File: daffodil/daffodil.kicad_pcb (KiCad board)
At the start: 2 copper layers, 70.7 x 53.3 mm, 8 parts, among them J1 NEIGHBOR1, J2 NEIGHBOR2, J7 BONUS_ROW, P1 GREATFET-PROTO-AREA

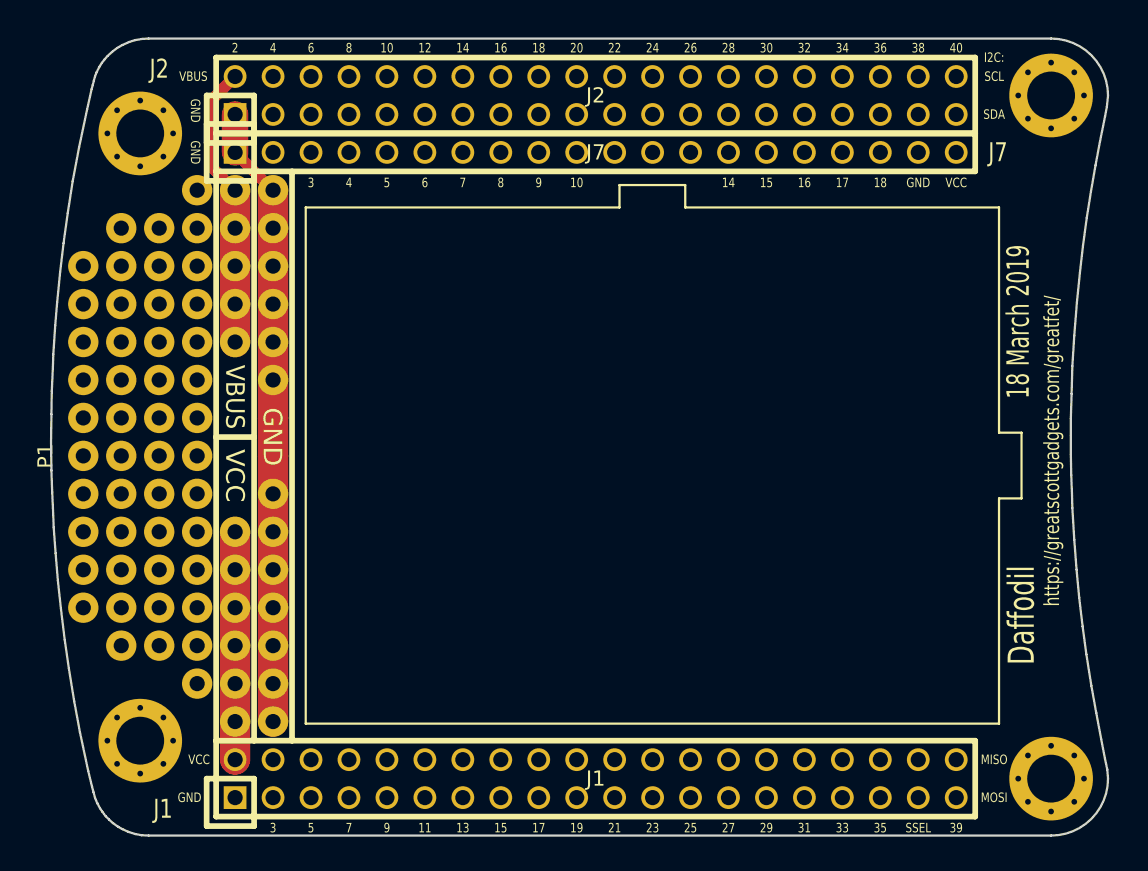
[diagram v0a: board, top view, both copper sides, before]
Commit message: Added a GND plain to to the top copper layer of Daffodil.
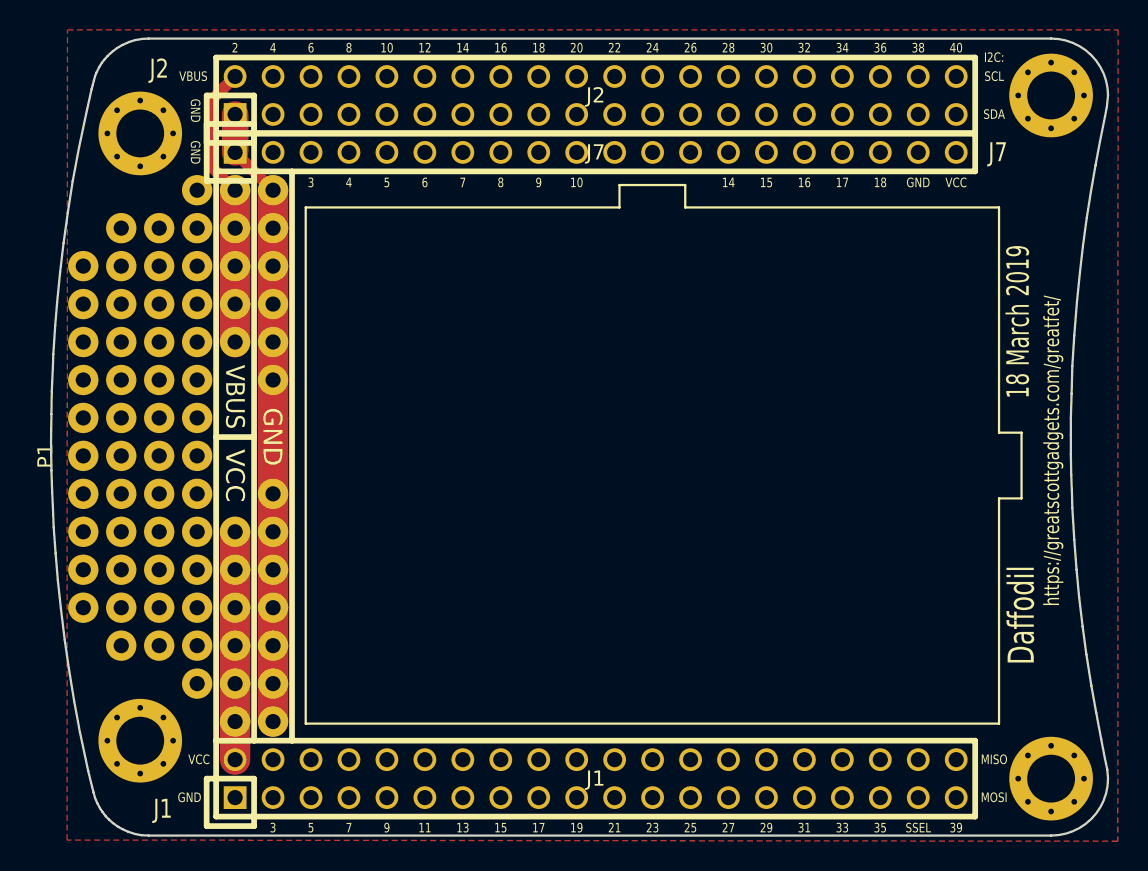
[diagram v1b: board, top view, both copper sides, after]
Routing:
- added copper zone on F.Cu, net GND

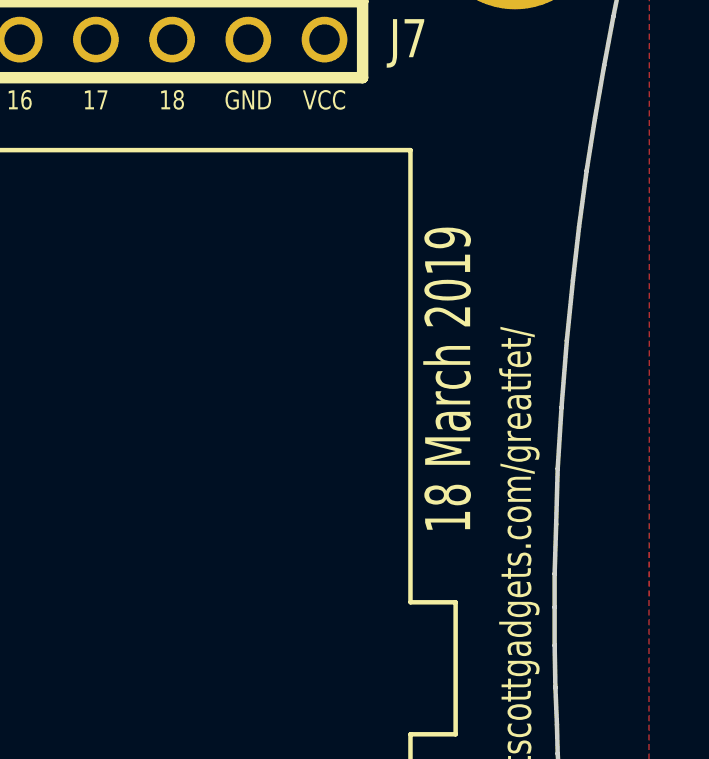
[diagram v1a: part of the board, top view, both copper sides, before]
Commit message: Updated date on Daffodil silkscreen.
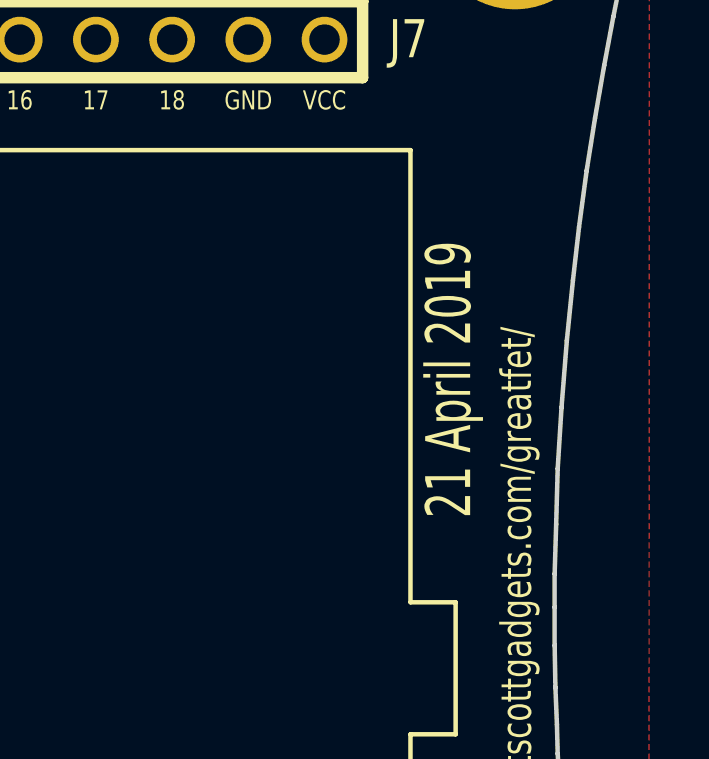
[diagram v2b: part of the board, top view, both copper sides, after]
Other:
- board text added: "21 April 2019"
- board text removed: "18 March 2019"
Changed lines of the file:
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@@
   (gr_line (start 177.9016 92.3544) (end 177.8508 94.0054) (angle 90) (layer Edge.Cuts) (width 0.15))
   (gr_line (start 177.9524 90.5002) (end 177.9016 92.3544) (angle 90) (layer Edge.Cuts) (width 0.15))
-  (gr_text "18 March 2019" (at 174.34 87.53 90) (layer F.SilkS)
+  (gr_text "21 April 2019" (at 174.34 87.53 90) (layer F.SilkS)
     (effects (font (size 1.5 1) (thickness 0.2)))
   )
